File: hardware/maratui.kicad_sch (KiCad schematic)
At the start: 5 parts, among them J1 Power Supply, J2 Lelit Mara, SW1 Button, U1 Ili9341_TFT_320x240

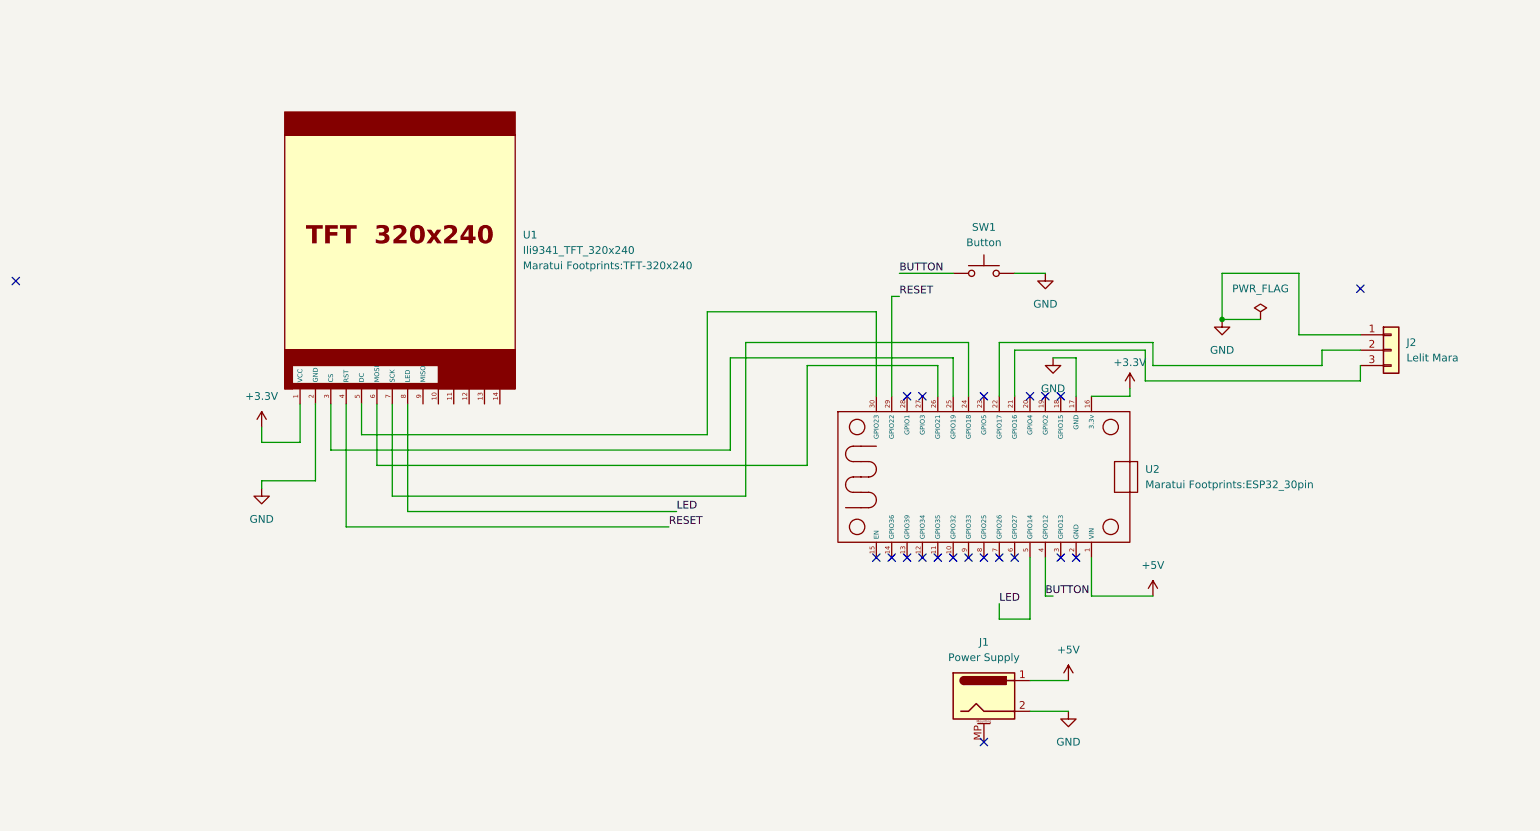
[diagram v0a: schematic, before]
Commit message: feat(hardware): scale-integrated board revision, 3D-printed scale mount
- Replace the board design (schematic, PCB, gerbers, .step) with the
  newer revision that includes the HX711 scale sockets — the previous
  files predated the scale feature entirely and no longer matched the
  firmware.
- Add hardware/lib/footprints/maratui.pretty/HX711_Socket.kicad_mod.
- Add hardware/3d-print/: printable case parts for the dual load-cell
  mount (doppelfuss = double foot, auflage_v2 = scale platform) as
  STEP/STL plus pre-sliced G-code.
- hardware/README.md: HX711 wiring table, 3s-hold calibration note, and
  a 3D-Printed Parts section; drop the stale gerbers/maratui-v1.zip
  reference in favor of the current gerbers.zip (base board) and
  260903_Platine_waage.zip (scale add-on board).

Co-Authored-By: Claude Sonnet 5 <noreply@anthropic.com>
Claude-Session: https://claude.ai/code/session_01Ko6obK5yneSFLNZKCRo7FE
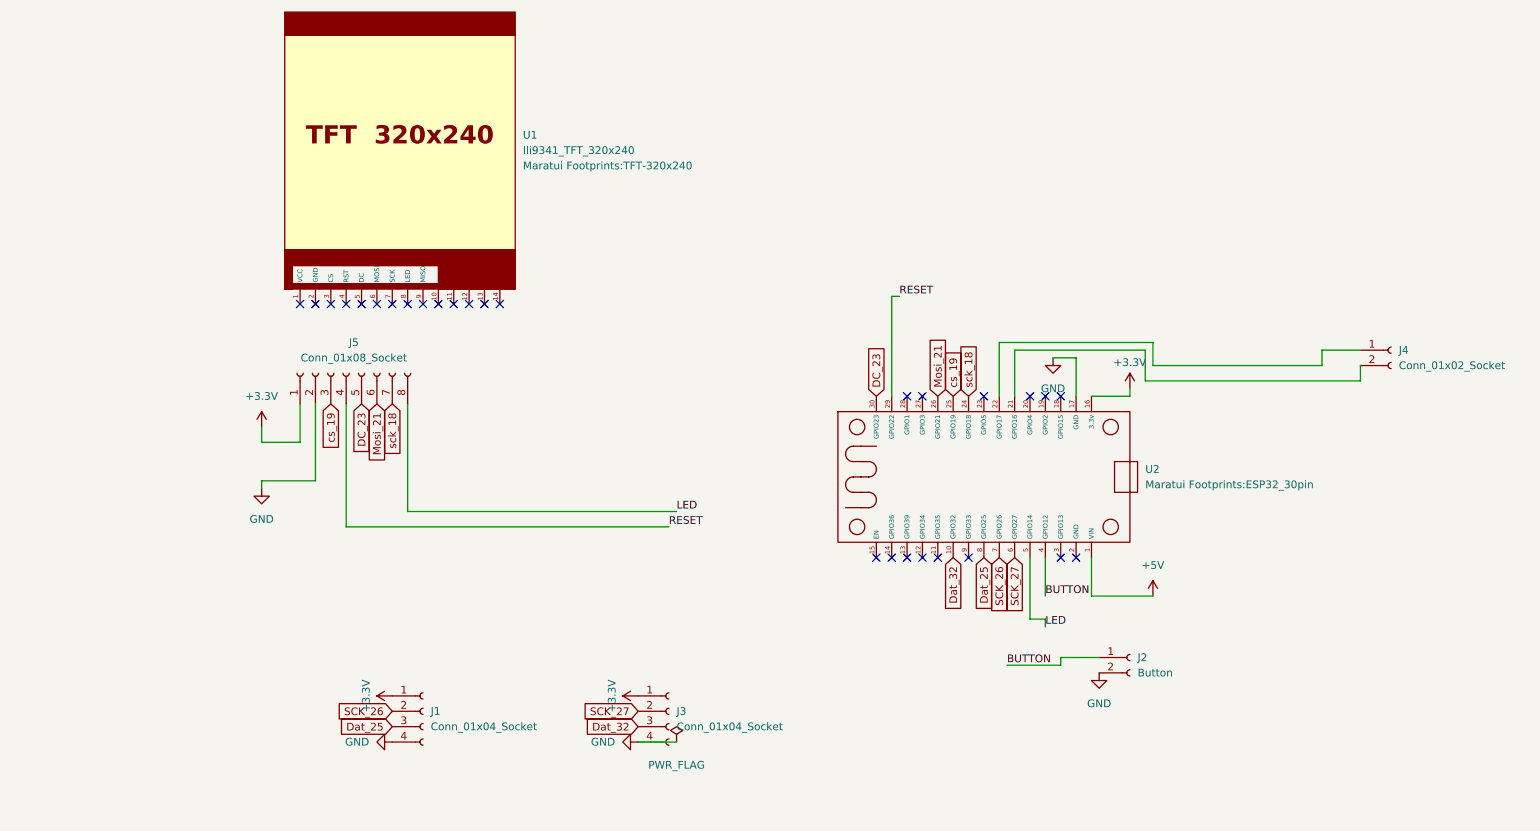
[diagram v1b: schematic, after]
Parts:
- removed J1: Power Supply, Connector_BarrelJack:BarrelJack_CUI_PJ-102AH_Horizontal, symbol Connector:Barrel_Jack_MountingPin
- removed J2: Lelit Mara, Connector_PinHeader_2.54mm:PinHeader_1x03_P2.54mm_Vertical, symbol Connector_Generic:Conn_01x03
- removed SW1: Button, Button_Switch_THT:SW_PUSH_6mm, symbol Switch:SW_Push
- added J1, J3: Conn_01x04_Socket, Connector_PinSocket_2.54mm:PinSocket_1x05_P2.54mm_Vertical, symbol Connector:Conn_01x04_Socket
- added J2: Button, Connector_JST:JST_EH_S2B-EH_1x02_P2.50mm_Horizontal, symbol Connector:Conn_01x02_Socket
- added J4: Conn_01x02_Socket, Connector_JST:JST_EH_S2B-EH_1x02_P2.50mm_Horizontal, symbol Connector:Conn_01x02_Socket
- added J5: Conn_01x08_Socket, Connector_PinSocket_2.54mm:PinSocket_1x08_P2.54mm_Vertical, symbol Connector:Conn_01x08_Socket
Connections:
- net +3.3V: now also J1.1 (Pin_1), J3.1 (Pin_1), J5.1 (Pin_1); no longer U1.1 (VCC)
- net BUTTON: now also J2.1 (Pin_1)
- net GND: now also J1.4 (Pin_4), J2.2 (Pin_2), J3.4 (Pin_4), J5.2 (Pin_2); no longer U1.2 (GND)
- net LED: now also J5.8 (Pin_8); no longer U1.8 (LED)
- net RESET: now also J5.4 (Pin_4); no longer U1.4 (RST)
- net at U1.3 (CS): no longer U2.25 (GPIO19)
- net at U1.5 (DC): no longer U2.30 (GPIO23)
- net at U1.6 (MOSI): no longer U2.26 (GPIO21)
- net at U1.7 (SCK): no longer U2.24 (GPIO18)
- net Dat_32: now reaches U2.10 (GPIO32)
- net Dat_32: now also J3.3 (Pin_3)
- net at U2.21 (GPIO16): now also J4.2 (Pin_2)
- net at U2.22 (GPIO17): now also J4.1 (Pin_1)
- net SCK_27: now reaches U2.6 (GPIO27)
- net SCK_27: now also J3.2 (Pin_2)
- net SCK_26: now reaches U2.7 (GPIO26)
- net SCK_26: now also J1.2 (Pin_2)
- net Dat_25: now reaches U2.8 (GPIO25)
- net Dat_25: now also J1.3 (Pin_3)
- new net DC_23: J5.5 (Pin_5), U2.30 (GPIO23)
- new net Mosi_21: J5.6 (Pin_6), U2.26 (GPIO21)
- new net cs_19: J5.3 (Pin_3), U2.25 (GPIO19)
- new net sck_18: J5.7 (Pin_7), U2.24 (GPIO18)
- no-connect marks 21 -> 28
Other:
- moved on the sheet: U1

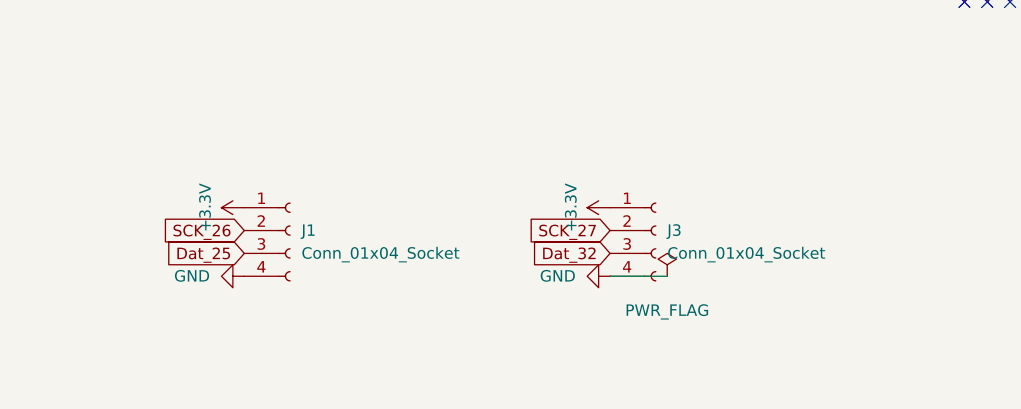
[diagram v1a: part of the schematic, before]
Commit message: hardware: update PCB and gerbers for the ordered board revision
Updated schematic/PCB and regenerated gerbers.zip for the board
revision that was ordered from fab. Removed the now-superseded
separate scale add-on gerber zip (260903_Platine_waage.zip) — the
scale cells are part of the single-board gerbers.zip export.

Co-Authored-By: Claude Sonnet 5 <noreply@anthropic.com>
Claude-Session: https://claude.ai/code/session_01Ko6obK5yneSFLNZKCRo7FE
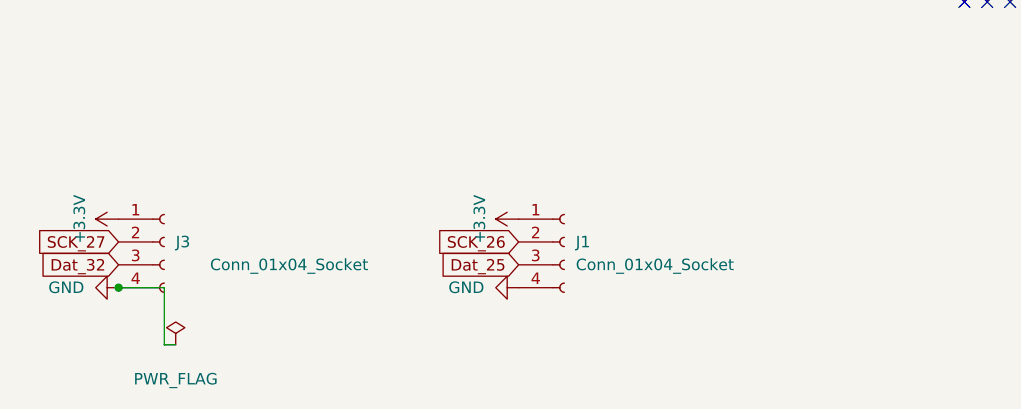
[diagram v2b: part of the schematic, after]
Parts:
- J2, J4: footprint Connector_JST:JST_EH_S2B-EH_1x02_P2.50mm_Horizontal -> Connector_JST:JST_EH_B2B-EH-A_1x02_P2.50mm_Vertical
- J5: footprint Connector_PinSocket_2.54mm:PinSocket_1x08_P2.54mm_Vertical -> Connector_PinSocket_2.54mm:PinSocket_1x14_P2.54mm_Vertical
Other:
- moved on the sheet: J1, J3

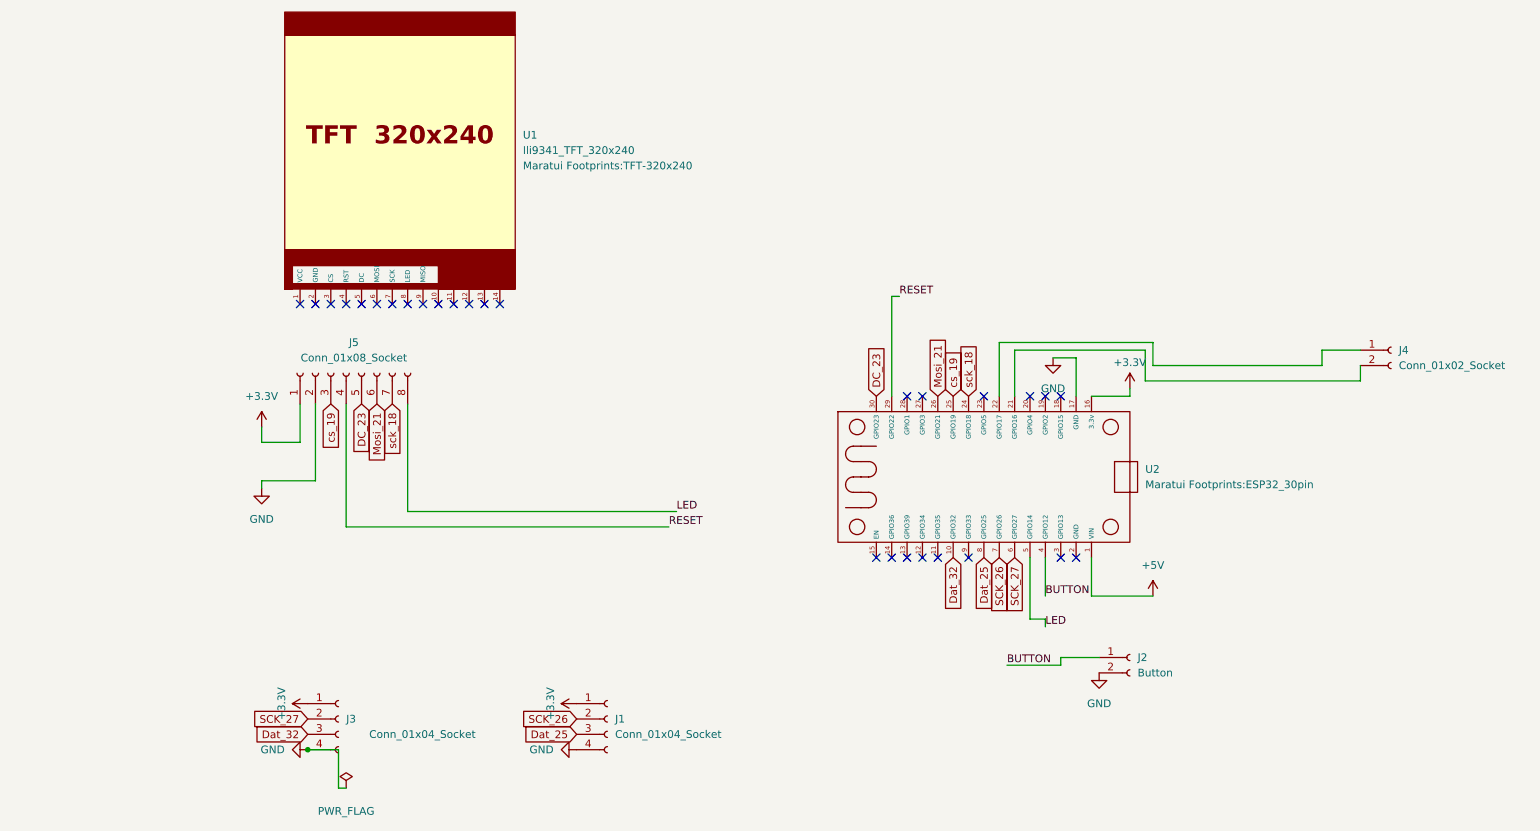
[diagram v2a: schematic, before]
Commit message: feat(hardware): rework schematic/PCB and reorganize KiCad library
Consolidates the ESP32, HX711 and TFT footprints/symbols/3D models into
a single hardware/lib/ tree (3dshapes, footprints.pretty, symbols),
replacing the old per-part library layout. Adds a BOM export (maratui.csv).

Co-Authored-By: Claude Sonnet 5 <noreply@anthropic.com>
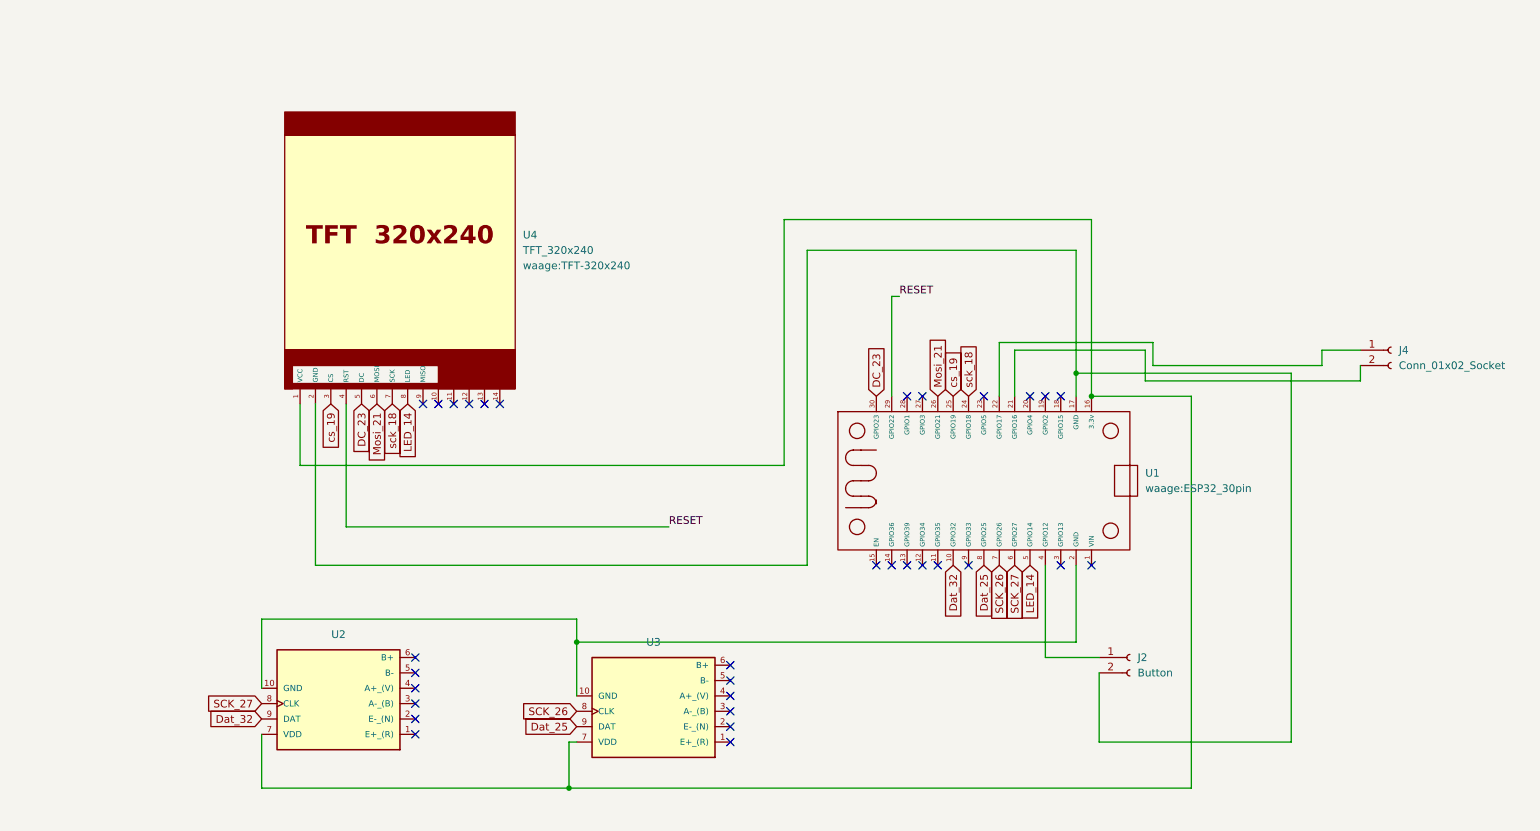
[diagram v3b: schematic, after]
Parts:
- removed J1, J3: Conn_01x04_Socket, Connector_PinSocket_2.54mm:PinSocket_1x05_P2.54mm_Vertical, symbol Connector:Conn_01x04_Socket
- removed J5: Conn_01x08_Socket, Connector_PinSocket_2.54mm:PinSocket_1x14_P2.54mm_Vertical, symbol Connector:Conn_01x08_Socket
- removed U1: Ili9341_TFT_320x240, Maratui Footprints:TFT-320x240, symbol ili9341_touch:TFT_320x240
- removed U2: (no value), Maratui Footprints:ESP32_30pin, symbol Esp32_30pin:ESP32_30Pin
- added U1: (no value), waage:ESP32_30pin, symbol Waage_Library:ESP32_30Pin
- added U2, U3: HX711, waage:HX711_module, symbol Waage_Library:HX711_module
- added U4: TFT_320x240, waage:TFT-320x240, symbol Waage_Library:TFT_320x240
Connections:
- net DC_23: now also U1.30 (GPIO23), U4.5 (DC)
- net Dat_25: now also U1.8 (GPIO25), U3.9 (DAT)
- net Dat_32: now also U1.10 (GPIO32), U2.9 (DAT)
- net Mosi_21: now also U1.26 (GPIO21), U4.6 (MOSI)
- net RESET: now also U1.29 (GPIO22), U4.4 (RST)
- net SCK_26: now also U1.7 (GPIO26), U3.8 (CLK)
- net SCK_27: now also U1.6 (GPIO27), U2.8 (CLK)
- net cs_19: now also U1.25 (GPIO19), U4.3 (CS)
- net sck_18: now also U1.24 (GPIO18), U4.7 (SCK)
- net at J4.2 (Pin_2): now also U1.21 (GPIO16)
- net at J4.1 (Pin_1): now also U1.22 (GPIO17)
- net BUTTON: no longer names the net of J2.1 (Pin_1)
- net BUTTON: now also U1.4 (GPIO12)
- net GND: no longer names the net of J2.2 (Pin_2)
- net GND: now also U1.17 (GND), U4.2 (GND)
- new net: U1.2 (GND), U2.10 (GND), U3.10 (GND)
- new net: U1.16 (3.3v), U2.7 (VDD), U3.7 (VDD), U4.1 (VCC)
- new net LED_14: U1.5 (GPIO14), U4.8 (LED)
- no-connect marks 28 -> 32
